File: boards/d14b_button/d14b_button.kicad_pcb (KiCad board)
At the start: 2 copper layers, 84 x 84 mm, 6 parts, among them SW1 SW_PUSH, SW2 SW_PUSH, U1 STM32F030F4P6TR, U2 nRF24L01+-Module

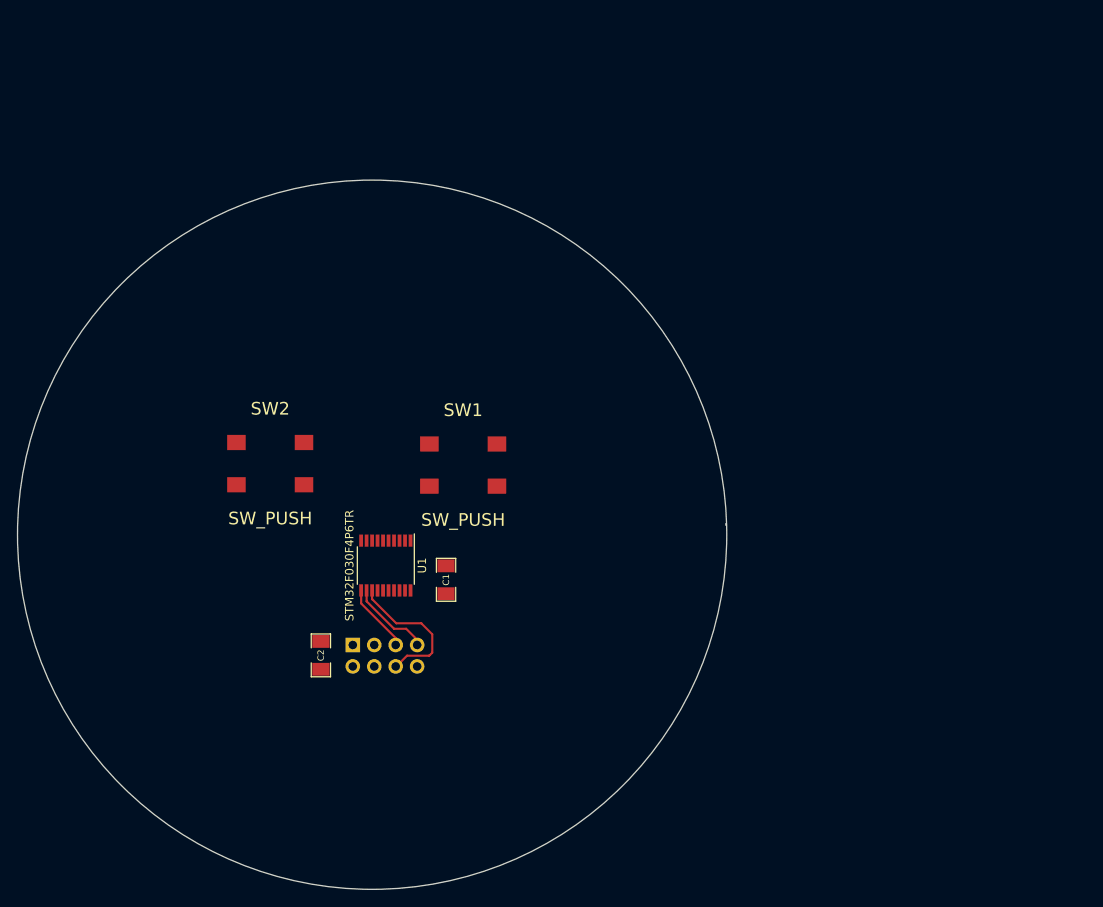
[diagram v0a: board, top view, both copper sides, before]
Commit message: Bauteile platziert
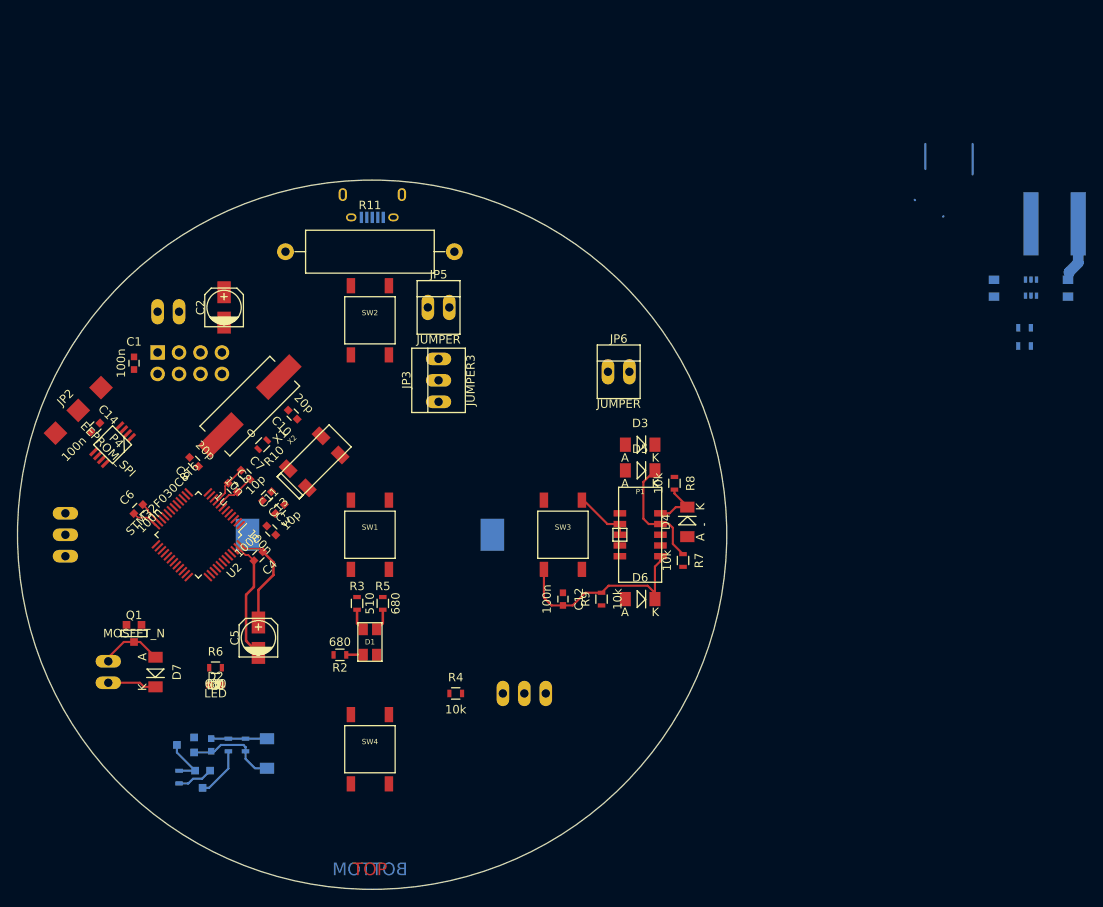
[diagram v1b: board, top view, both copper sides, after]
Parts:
- added BT1: BATTERY, batteryconn:KZH20SMD-2, B.Cu at (152.9, 105.2)
- added C10: 20p, Capacitors_SMD:C_0603, F.Cu at (143.8, 90.9)
- added C11: 10p, Capacitors_SMD:C_0603, F.Cu at (142.2, 102.1)
- added C12: 100n, Capacitors_SMD:C_0603, F.Cu at (175.8, 112.8)
- added C13: 10p, Capacitors_SMD:C_0603, F.Cu at (140.7, 100.6)
- added C14: 100n, Capacitors_SMD:C_0603, F.Cu at (120.4, 92.5)
- added C15: 10u, Capacitors_SMD:C_0805, B.Cu at (235.6, 75.9)
- added C16: 10u, Capacitors_SMD:C_0805, B.Cu at (226.8, 75.9)
- added C17: 100n, Capacitors_SMD:C_0603, B.Cu at (134.1, 130.0)
- added C3: 100n, Capacitors_SMD:C_0603, F.Cu at (141.2, 104.6)
- added C4: 100n, Capacitors_SMD:C_0603, F.Cu at (139.7, 107.7)
- added C5: 4.7u, Capacitors_SMD:c_elec_4x5.8, F.Cu at (139.7, 117.3)
- added C6: 100n, Capacitors_SMD:C_0603, F.Cu at (125.5, 102.1)
- added C7: 10n, Capacitors_SMD:C_0603, F.Cu at (138.2, 98.0)
- added C8: 1u, Capacitors_SMD:C_0603, F.Cu at (136.7, 99.6)
- added C9: 20p, Capacitors_SMD:C_0603, F.Cu at (132.1, 96.5)
- added CON1: USB-MICRO-B, Connect:USB_Micro-B, B.Cu at (151.9, 67.6)
- added D1: LED_RABG, d14lib:PLCC-4, F.Cu at (152.9, 117.9)
- added D2: LED, LEDs:LED-0603, F.Cu at (134.6, 122.9)
- added D3: Z5V1, Diodes_SMD:Diode-MiniMELF_Standard, F.Cu at (184.9, 94.5)
- added D4: Z5V1, Diodes_SMD:Diode-MiniMELF_Standard, F.Cu at (190.5, 103.6)
- added D5: Z5V1, Diodes_SMD:Diode-MiniMELF_Standard, F.Cu at (184.9, 97.5)
- added D6: Z5V1, Diodes_SMD:Diode-MiniMELF_Standard, F.Cu at (184.9, 112.8)
- added D7: DIODE, Diodes_SMD:Diode-MiniMELF_Standard, F.Cu at (127.5, 121.4)
- added D8: ZENERsmall, Diodes_SMD:Diode-MiniMELF_Standard, B.Cu at (140.7, 131.1)
- added JP1: JUMPER3, Connect:PINHEAD1-3, B.Cu at (171.2, 124.0)
- added JP2: JUMPER3, Oddities:NetTie-II_SMD, F.Cu at (118.4, 90.4)
- added JP3: JUMPER3, Connect:PINHEAD1-3, F.Cu at (161.0, 86.9)
- added JP4: JUMPER, Connect:PINHEAD1-2, B.Cu at (129.0, 78.7)
- added JP5: JUMPER, Connect:PINHEAD1-2, F.Cu at (161.0, 78.2)
- added JP6: JUMPER, Connect:PINHEAD1-2, F.Cu at (182.4, 85.9)
- added L1: 4.7u, d14lib:NRS8030, B.Cu at (234.0, 68.3)
- added P1: CONN_02X05, d14lib:CORTEX_header_SMD, F.Cu at (184.9, 105.2)
- added P2: CONN_01X03, Connect:PINHEAD1-3, B.Cu at (116.8, 105.2)
- added P3: PIEZO_BUZZ, Connect:PINHEAD1-2, B.Cu at (121.9, 121.4)
- added P4: EEPROM_SPI, SMD_Packages:MSOP-8, F.Cu at (122.4, 94.5)
- added Q1: MOSFET_N, SMD_Packages:SOT-23-GDS, F.Cu at (125.0, 116.8)
- added Q2: IRLM6402, SMD_Packages:SOT-23-GDS, B.Cu at (133.1, 134.1)
- added Q3: BSS138, SMD_Packages:SOT-23-GDS, B.Cu at (131.1, 130.0)
- added R1: 100k, Resistors_SMD:R_0603, B.Cu at (130.3, 133.9)
- added R10: 0, Resistors_SMD:R_0603, F.Cu at (140.2, 94.5)
- added R11: 10, 2.5W, Resistors_ThroughHole:Resistor_Horizontal_RM20mm, F.Cu at (152.9, 71.6)
- added R12: 0, Resistors_SMD:R_0603, B.Cu at (230.4, 80.6)
- added R13: *, Resistors_SMD:R_0603, B.Cu at (230.4, 82.8)
- added R14: 10k, Resistors_SMD:R_0603, B.Cu at (136.1, 130.0)
- added R15: 10k, Resistors_SMD:R_0603, B.Cu at (138.2, 130.0)
- added R2: 680, Resistors_SMD:R_0603, F.Cu at (149.4, 119.4)
- added R3: 510, Resistors_SMD:R_0603, F.Cu at (151.4, 113.3)
- added R4: 10k, Resistors_SMD:R_0603, F.Cu at (163.1, 124.0)
- added R5: 680, Resistors_SMD:R_0603, F.Cu at (154.4, 113.3)
- added R6: 680, Resistors_SMD:R_0603, F.Cu at (134.6, 120.9)
- added R7: 10k, Resistors_SMD:R_0603, F.Cu at (190.0, 108.2)
- added R8: 10k, Resistors_SMD:R_0603, F.Cu at (189.0, 99.1)
- added R9: 10k, Resistors_SMD:R_0603, F.Cu at (180.3, 112.8)
- added SW3: SW_PUSH, d14lib:Button_SMD_Schurter_LSG, F.Cu at (175.8, 105.2)
- added SW4: SW_PUSH, d14lib:Button_SMD_Schurter_LSG, F.Cu at (152.9, 130.6)
- added U3: TPS61221, Housings_SOT-23_SOT-143_TSOT-6:SC70-6, B.Cu at (231.2, 75.9)
- added X1: 8M, Crystals:Crystal_HC49-SD_SMD, F.Cu at (138.7, 89.9)
- added X2: 32.768k, d14lib:crystal_SMD_CPFB, F.Cu at (146.3, 96.5)
- C1: footprint SMD_Packages:SMD-1206 -> Capacitors_SMD:C_0603
- C2: footprint SMD_Packages:SMD-1206 -> Capacitors_SMD:c_elec_4x5.8
- SW1, SW2: footprint d14b_libs:TACTILE_SW -> d14lib:Button_SMD_Schurter_LSG
- U1: value STM32F030F4P6TR -> nRF24L01+-Module; footprint Housings_SSOP:TSSOP-20_4.4x6.5mm_Pitch0.65mm -> Pin_Headers:Pin_Header_Straight_2x04; moved to B.Cu
- U2: value nRF24L01+-Module -> STM32F030C8T6; footprint Pin_Headers:Pin_Header_Straight_2x04 -> Housings_QFP:LQFP-48_7x7mm_Pitch0.5mm; moved to F.Cu
- moved C1 45.0 mm to (125.0, 84.8), turned to 90 degrees
- moved C2 42.8 mm to (135.6, 78.2)
- moved U1 33.4 mm to (131.6, 84.8), turned to 0 degrees
- moved U2 26.3 mm to (132.6, 105.2), turned to 225 degrees
- moved SW2 21.1 mm to (152.9, 79.8)
- moved SW1 13.5 mm to (152.9, 105.2)
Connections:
- C1 pad 1: 3V3 -> Net-(C1-Pad1)
- C2 pad 1: 3V3 -> Net-(C1-Pad1)
- SW1 pad 2: 3V3 -> +3V3
- SW2 pad 2: 3V3 -> +3V3
- U1 pad 1: Net-(U1-Pad1) -> GND
- U1 pad 2: Net-(U1-Pad2) -> Net-(C1-Pad1)
- U1 pad 3: Net-(U1-Pad3) -> /CE
- U1 pad 4: Net-(U1-Pad4) -> /CSN
- U1 pad 5: Net-(U1-Pad5) -> /SCK
- U1 pad 6: Net-(SW1-Pad1) -> /MOSI
- U1 pad 7: Net-(SW2-Pad1) -> /MISO
- U1 pad 8: Net-(U1-Pad8) -> /IRQ
- U2 pad 1: GND -> +3V3
- U2 pad 2: 3V3 -> (no net)
- U2 pad 3: CE -> Net-(C11-Pad1)
- U2 pad 4: CSN -> Net-(C13-Pad1)
- U2 pad 5: SCK -> Net-(C9-Pad2)
- U2 pad 6: MOSI -> Net-(R10-Pad2)
- U2 pad 7: MISO -> /NRST
- U2 pad 8: IRQ -> GND
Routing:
- net GND: track 0.00 -> 40.1 mm
- net +3V3: track 0.00 -> 26.5 mm
- net /NRST: track 0.00 -> 24.3 mm
- net MOSI: track 17.1 -> 0.00 mm
- net /SWCLK: track 0.00 -> 13.8 mm
- net MISO: track 9.78 -> 0.00 mm
- net SCK: track 8.16 -> 0.00 mm
- net Net-(D7-Pad1): track 0.00 -> 7.54 mm
- net Net-(C15-Pad1): track 0.00 -> 7.12 mm
- net (no net): track 0.00 -> 6.73 mm
- net /DIV_MEAS: track 0.00 -> 6.61 mm
- net /SWDIO: track 0.00 -> 6.20 mm
- net Net-(Q2-PadD): track 0.00 -> 6.04 mm
- net Net-(Q2-PadG): track 0.00 -> 5.85 mm
- net /VSUP_MEAS: track 0.00 -> 4.31 mm
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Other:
- outline, holes or cut-outs redrawn
- net class Default: via_dia 0.889 -> 2.5; via_drill 0.635 -> 0.9
- rule trace_min: 0.254 -> 0.2032
- rule via_min_drill: 0.508 -> 0.9
- rule via_min_size: 0.889 -> 2.5
- board text added: "BOTTOM"
- board text added: "TOP"

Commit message: Layoutzwischenstand
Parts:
- moved C15 65.9 mm to (169.7, 79.1), turned to 90 degrees
- moved L1 65.3 mm to (171.3, 86.7), turned to 0 degrees
- moved U3 57.2 mm to (174.1, 79.2), turned to 0 degrees
- moved R13 56.6 mm to (174.9, 72.3), turned to 0 degrees
- moved R12 55.9 mm to (174.9, 74.4), turned to 180 degrees
- moved C16 48.4 mm to (178.5, 79.1), turned to 90 degrees
- moved C6 0.81 mm to (125.1, 102.8)
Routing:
- net /DIV_MEAS: track 6.61 -> 78.4 mm, vias 0 -> 1
- net GND: track 40.1 -> 106.0 mm, vias 0 -> 2
- net Net-(C16-Pad1): track 0.34 -> 29.7 mm
- net Net-(CON1-Pad1): track 0.00 -> 27.3 mm
- net /VSUP_MEAS: track 4.31 -> 28.4 mm
- net Net-(C15-Pad1): track 7.12 -> 29.4 mm
- net Net-(BT1-Pad1): track 0.00 -> 18.4 mm
- net Net-(CON1-Pad5): track 0.00 -> 16.6 mm
- net /UARTTX: track 0.00 -> 14.6 mm
- net /UARTRX: track 0.00 -> 14.2 mm
- net /ROM_HOLD: track 0.00 -> 13.4 mm
- net +3V3: track 26.5 -> 39.1 mm
- net Net-(L1-Pad2): track 0.02 -> 12.5 mm
- net /MOSI: track 0.00 -> 12.3 mm
- net Net-(JP2-Pad2): track 0.00 -> 7.01 mm
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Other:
- net class Default: clearance 0.254 -> 0.2032
- rule trace_clearance: 0.254 -> 0.2032

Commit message: weiterer Zwischenstand
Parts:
- moved C1 3.77 mm to (126.4, 81.4)
- moved C2 3.77 mm to (137.1, 74.8), turned to 270 degrees
- moved JP4 3.77 mm to (130.5, 75.3)
- moved U1 3.77 mm to (133.0, 81.4)
- moved R10 1.24 mm to (141.0, 93.5)
- moved C7 0.84 mm to (137.5, 97.6)
- moved C8 0.79 mm to (136.1, 99.0)
- turned C13 to 45 degrees
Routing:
- net /SWDIO: track 6.20 -> 115.9 mm
- net /VSUP_MEAS: track 28.4 -> 131.8 mm
- net /SWCLK: track 13.8 -> 113.6 mm
- net /NRST: track 24.3 -> 81.9 mm, vias 0 -> 2
- net GND: track 106.0 -> 163.1 mm, vias 2 -> 4
- net Net-(SW4-Pad1): track 0.00 -> 47.5 mm
- net +3V3: track 39.1 -> 85.0 mm, vias 0 -> 1
- net Net-(R6-Pad2): track 0.00 -> 39.2 mm, vias 0 -> 2
- net /SCK: track 0.00 -> 32.4 mm, vias 0 -> 2
- net /ROM_CS: track 0.02 -> 31.9 mm, vias 0 -> 2
- net /MEAS_ENABLE: track 0.00 -> 31.3 mm, vias 0 -> 1
- net Net-(SW1-Pad1): track 0.00 -> 25.8 mm, vias 0 -> 2
- net Net-(C9-Pad2): track 0.00 -> 22.9 mm
- net Net-(Q1-PadG): track 0.00 -> 20.1 mm, vias 0 -> 2
- net Net-(C1-Pad1): track 0.00 -> 18.7 mm
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
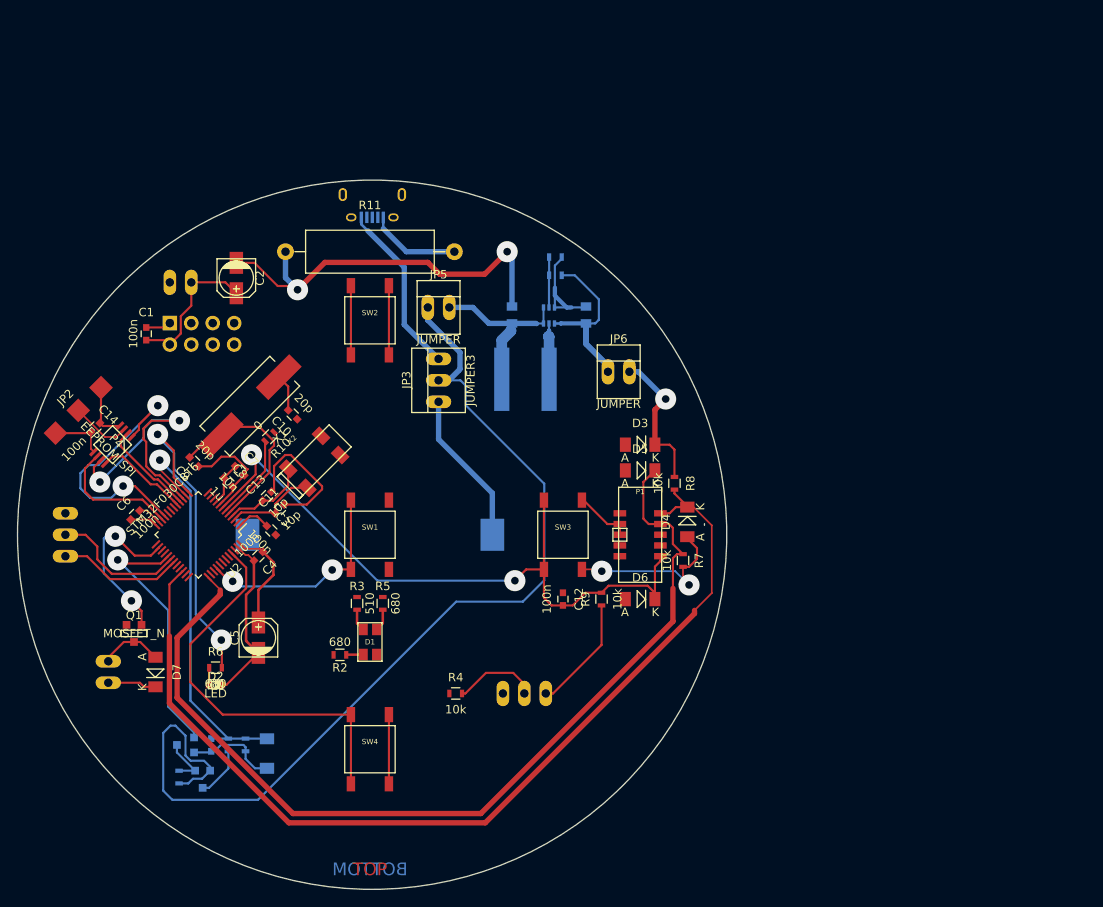
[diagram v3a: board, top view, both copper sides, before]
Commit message: Fiebermurks verworfen, Redesign der Platine angeworfen, Interactive Routing ist geil :-)
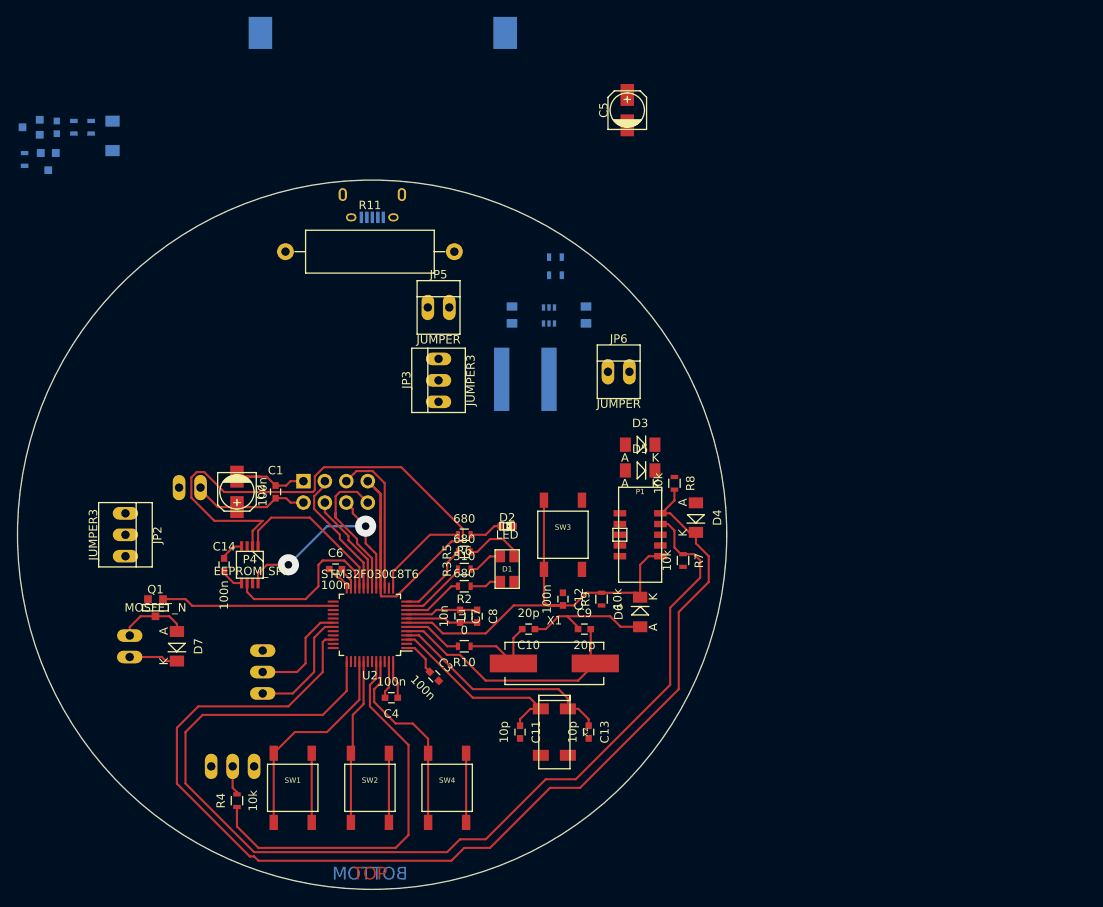
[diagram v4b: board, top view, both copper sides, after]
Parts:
- JP2: footprint Oddities:NetTie-II_SMD -> Connect:PINHEAD1-3
- moved C5 76.2 mm to (183.4, 54.9)
- moved C17 75.4 mm to (115.8, 56.9)
- moved Q3 75.4 mm to (112.8, 56.9)
- moved R1 75.4 mm to (112.0, 60.7)
- moved R14 75.4 mm to (117.9, 56.9)
- moved D8 75.4 mm to (122.4, 57.9)
- moved Q2 75.4 mm to (114.8, 61.0)
- moved R15 75.4 mm to (119.9, 56.9)
- moved BT1 59.5 mm to (154.4, 45.7)
- moved SW2 55.4 mm to (152.9, 135.1)
- moved C9 50.3 mm to (178.3, 116.3), turned to 0 degrees
- moved C13 47.2 mm to (178.8, 128.5), turned to 270 degrees
- moved X1 47.2 mm to (174.8, 120.4), turned to 0 degrees
- moved X2 42.8 mm to (174.8, 128.5), turned to 270 degrees
- moved D2 39.3 mm to (169.2, 104.1)
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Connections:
- U2 pad 18: /CE -> /IRQ
- U2 pad 20: /IRQ -> /CE
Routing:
- net /VSUP_MEAS: track 131.8 -> 0.00 mm
- net GND: track 163.1 -> 45.5 mm, vias 4 -> 0
- net /MISO: track 11.6 -> 96.3 mm
- net /DIV_MEAS: track 78.4 -> 0.00 mm, vias 1 -> 0
- net Net-(R4-Pad1): track 0.00 -> 47.0 mm
- net /MEAS_ENABLE: track 31.3 -> 0.00 mm, vias 1 -> 0
- net +3V3: track 85.0 -> 54.0 mm, vias 1 -> 0
- net Net-(C16-Pad1): track 29.7 -> 0.00 mm
- net /NRST: track 81.9 -> 52.2 mm, vias 2 -> 0
- net Net-(C15-Pad1): track 29.4 -> 0.00 mm
- net Net-(R6-Pad2): track 39.2 -> 11.4 mm, vias 2 -> 0
- net Net-(CON1-Pad1): track 27.3 -> 0.00 mm
- net Net-(SW4-Pad1): track 47.5 -> 23.2 mm
- net Net-(BT1-Pad1): track 18.4 -> 0.00 mm
- net /IRQ: track 0.00 -> 18.2 mm
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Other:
- outline, holes or cut-outs redrawn
